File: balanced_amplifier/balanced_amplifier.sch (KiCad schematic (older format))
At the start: 11 parts, among them J1 Conn_01x04_Male, J2 Conn_01x04_Male, J3 Screw_Terminal_01x03, J4 Conn_01x04_Male, J5 Conn_01x04_Male

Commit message: update balanced amplifier TODO and swap power connector for molex SL
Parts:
- removed J3: Screw_Terminal_01x03, TerminalBlock_Phoenix:TerminalBlock_Phoenix_PT-1,5-3-5.0-H_1x03_P5.00mm_Horizontal, symbol Connector:Screw_Terminal_01x03
- added J3: Conn_01x03_Male, symbol Connector:Conn_01x03_Male
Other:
- note added: "Mounting holes for 8-32 standoffs\nUse isolated standoffs"
- note added: "TODO:\nswap +/- for either input or output connectors (make consistent)\ncheck pinning of power connector matches power supply\nUpdate date field\nAdd power LED(s)\nchange connectors to support headphone amplifier board"
- note removed: "Mounting holes for 8-32 standoffs"
- note removed: "TODO:\nadd knobs for pots\nswap +/- for either input or output connectors (make consistent)\nchange power connector to 1x3 Molex SL\nUpdate date field\nAdd power LED(s)\nchange connectors to support headphone amplifier board\nshould mounting holes be tied to GNDA?"
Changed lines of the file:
@@
-$EndComp
-$Comp
-L Connector:Screw_Terminal_01x03 J3
-U 1 1 5C512EBE
-P 1400 5300
-F 0 "J3" H 1400 5500 50  0000 C CNN
-F 1 "Screw_Terminal_01x03" H 1400 5050 50  0000 C CNN
-F 2 "TerminalBlock_Phoenix:TerminalBlock_Phoenix_PT-1,5-3-5.0-H_1x03_P5.00mm_Horizontal" H 1400 5300 50  0001 C CNN
-F 3 "https://media.digikey.com/pdf/Data%20Sheets/Phoenix%20Contact%20PDFs/1935174.pdf" H 1400 5300 50  0001 C CNN
-F 4 "Phoenix" H 1400 5300 50  0001 C CNN "Manufacturer"
-F 5 "1935174" H 1400 5300 50  0001 C CNN "Manufacturer PN"
-F 6 "Digikey" H 1400 5300 50  0001 C CNN "Distributor"
-F 7 "277-1578-ND" H 1400 5300 50  0001 C CNN "Distributor PN"
-F 8 "https://www.digikey.com/product-detail/en/phoenix-contact/1935174/277-1578-ND/568615" H 1400 5300 50  0001 C CNN "URL"
-F 9 "0.60" H 1400 5300 50  0001 C CNN "Unit Price"
-	1    1400 5300
-	-1   0    0    1
 $EndComp
 $Comp
@@
 	9300 3450 9200 3450
 Text Notes 900  1500 0    50   ~ 0
-TODO:\nadd knobs for pots\nswap +/- for either input or output connectors (make consistent)\nchange power connector to 1x3 Molex SL\nUpdate date field\nAdd power LED(s)\nchange connectors to support headphone amplifier board\nshould mounting holes be tied to GNDA?
+TODO:\nswap +/- for either input or output connectors (make consistent)\ncheck pinning of power connector matches power supply\nUpdate date field\nAdd power LED(s)\nchange connectors to support headphone amplifier board
 Text Label 1450 2600 0    50   ~ 0
 right_in_hot
@@
 $EndComp
 Text Notes 7850 5450 0    50   ~ 0
-Mounting holes for 8-32 standoffs
+Mounting holes for 8-32 standoffs\nUse isolated standoffs
+$Comp
+L Connector:Conn_01x03_Male J3
+U 1 1 5CFE6E45
+P 1400 5300
+F 0 "J3" H 1372 5232 50  0000 R CNN
+F 1 "Conn_01x03_Male" H 1372 5323 50  0000 R CNN
+F 2 "" H 1400 5300 50  0001 C CNN
+F 3 "~" H 1400 5300 50  0001 C CNN
+	1    1400 5300
+	1    0    0    1
+$EndComp
 $EndSCHEMATC

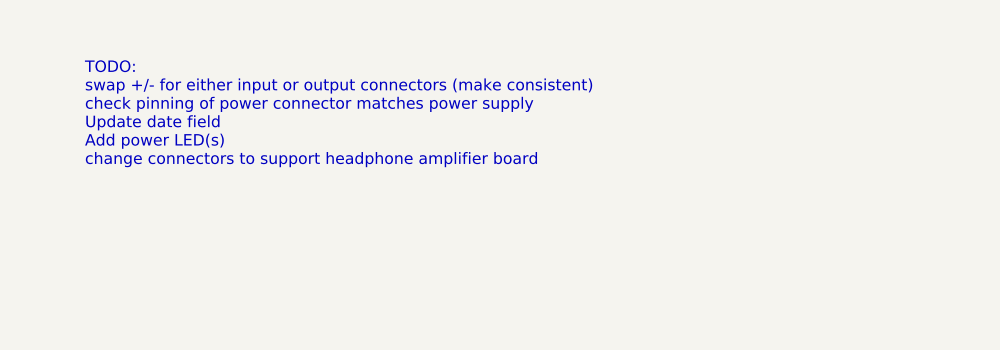
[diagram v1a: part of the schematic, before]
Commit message: update balanced amplifier TODO
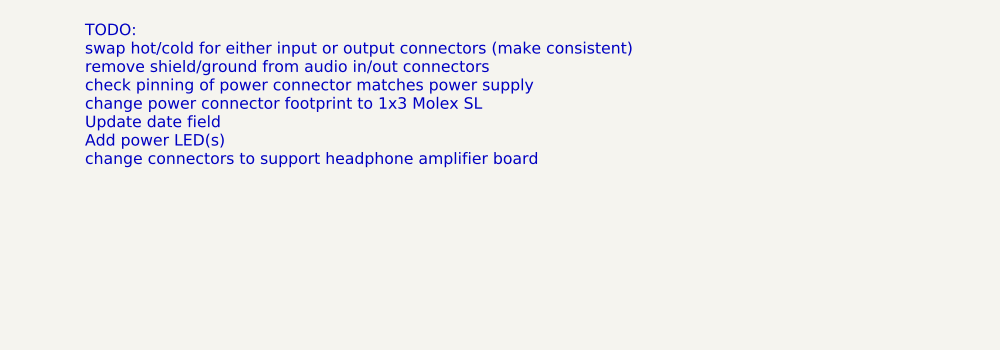
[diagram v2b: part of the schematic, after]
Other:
- note added: "TODO:\nswap hot/cold for either input or output connectors (make consistent)\nremove shield/ground from audio in/out connectors\ncheck pinning of power connector matches power supply\nchange power connector footprint to 1x3 Molex SL\nUpdate date field\nAdd power LED(s)\nchange connectors to support headphone amplifier board"
- note removed: "TODO:\nswap +/- for either input or output connectors (make consistent)\ncheck pinning of power connector matches power supply\nUpdate date field\nAdd power LED(s)\nchange connectors to support headphone amplifier board"
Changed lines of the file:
@@
 	9300 3450 9200 3450
 Text Notes 900  1500 0    50   ~ 0
-TODO:\nswap +/- for either input or output connectors (make consistent)\ncheck pinning of power connector matches power supply\nUpdate date field\nAdd power LED(s)\nchange connectors to support headphone amplifier board
+TODO:\nswap hot/cold for either input or output connectors (make consistent)\nremove shield/ground from audio in/out connectors\ncheck pinning of power connector matches power supply\nchange power connector footprint to 1x3 Molex SL\nUpdate date field\nAdd power LED(s)\nchange connectors to support headphone amplifier board
 Text Label 1450 2600 0    50   ~ 0
 right_in_hot

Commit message: update balanced amplifier input/output/power connectors
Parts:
- removed J2, J4, J5: Conn_01x04_Male, Connector_Molex_SL:Molex_SL_A-70543-0003_1x04_P2.54mm_Vertical, symbol Connector:Conn_01x04_Male
- removed J3: Conn_01x03_Male, symbol Connector:Conn_01x03_Male
- added J2, J4, J5, J6, J7: Molex_SL_01x02_Male, Connector_Molex_SL:Molex_SL_A-70543-0001_1x02_P2.54mm_Vertical, symbol Connector_gkeeth:Molex_SL_01x02_Male
- added J3: Molex_SL_01x03_Male, Connector_Molex_SL:Molex_SL_A-70543-0002_1x03_P2.54mm_Vertical, symbol Connector_gkeeth:Molex_SL_01x03_Male
- J1: value Conn_01x04_Male -> Molex_SL_01x02_Male; footprint Connector_Molex_SL:Molex_SL_A-70543-0003_1x04_P2.54mm_Vertical -> Connector_Molex_SL:Molex_SL_A-70543-0001_1x02_P2.54mm_Vertical; symbol Connector:Conn_01x04_Male -> Connector_gkeeth:Molex_SL_01x02_Male; Distributor PN WM4802-ND -> (none); Manufacturer PN 0705430003 -> 0705430001; URL https://www.digikey.com/products/en?keywords=0705430003 -> (none); Unit Price 0.99 -> (none)
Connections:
- net GNDA: now also J3.2 (Pin_2)
- net VCC: now also J3.1 (Pin_1)
- net VEE: now also J3.3 (Pin_3)
- net left_in_cold: now also J2.2 (Pin_2)
- net left_in_hot: now also J2.1 (Pin_1)
- net right_in_cold: now also J1.2 (Pin_2); no longer J1.4 (Pin_4)
- removed net right_in_ground: J1.2 (Pin_2), J1.3 (Pin_3)
- new net left_out_cold: J6.2 (Pin_2), J7.2 (Pin_2)
- new net left_out_hot: J6.1 (Pin_1), J7.1 (Pin_1)
- new net right_out_cold: J4.2 (Pin_2), J5.2 (Pin_2)
- new net right_out_hot: J4.1 (Pin_1), J5.1 (Pin_1)
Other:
- note added: "MOUNTING HOLES"
- note added: "TODO:\nUpdate date field\nAdd power LED(s)"
- note added: "Use insulating 8-32 standoffs"
- note added: "duplicate output connectors for\ninput/output board and headphone amplifier board"
- note added: "hot/cold outputs swapped to maintain overall phase\n(volume control inverts)"
- note removed: "Mounting holes for 8-32 standoffs\nUse isolated standoffs"
- note removed: "TODO:\nswap hot/cold for either input or output connectors (make consistent)\nremove shield/ground from audio in/out connectors\ncheck pinning of power connector matches power supply\nchange power connector footprint to 1x3 Molex SL\nUpdate date field\nAdd power LED(s)\nchange connectors to support headphone amplifier board"
- note removed: "hot/cold inputs swapped to maintain overall phase\n(volume control inverts)"
- moved on the sheet: C100, C101, H1, H2, H3, H4

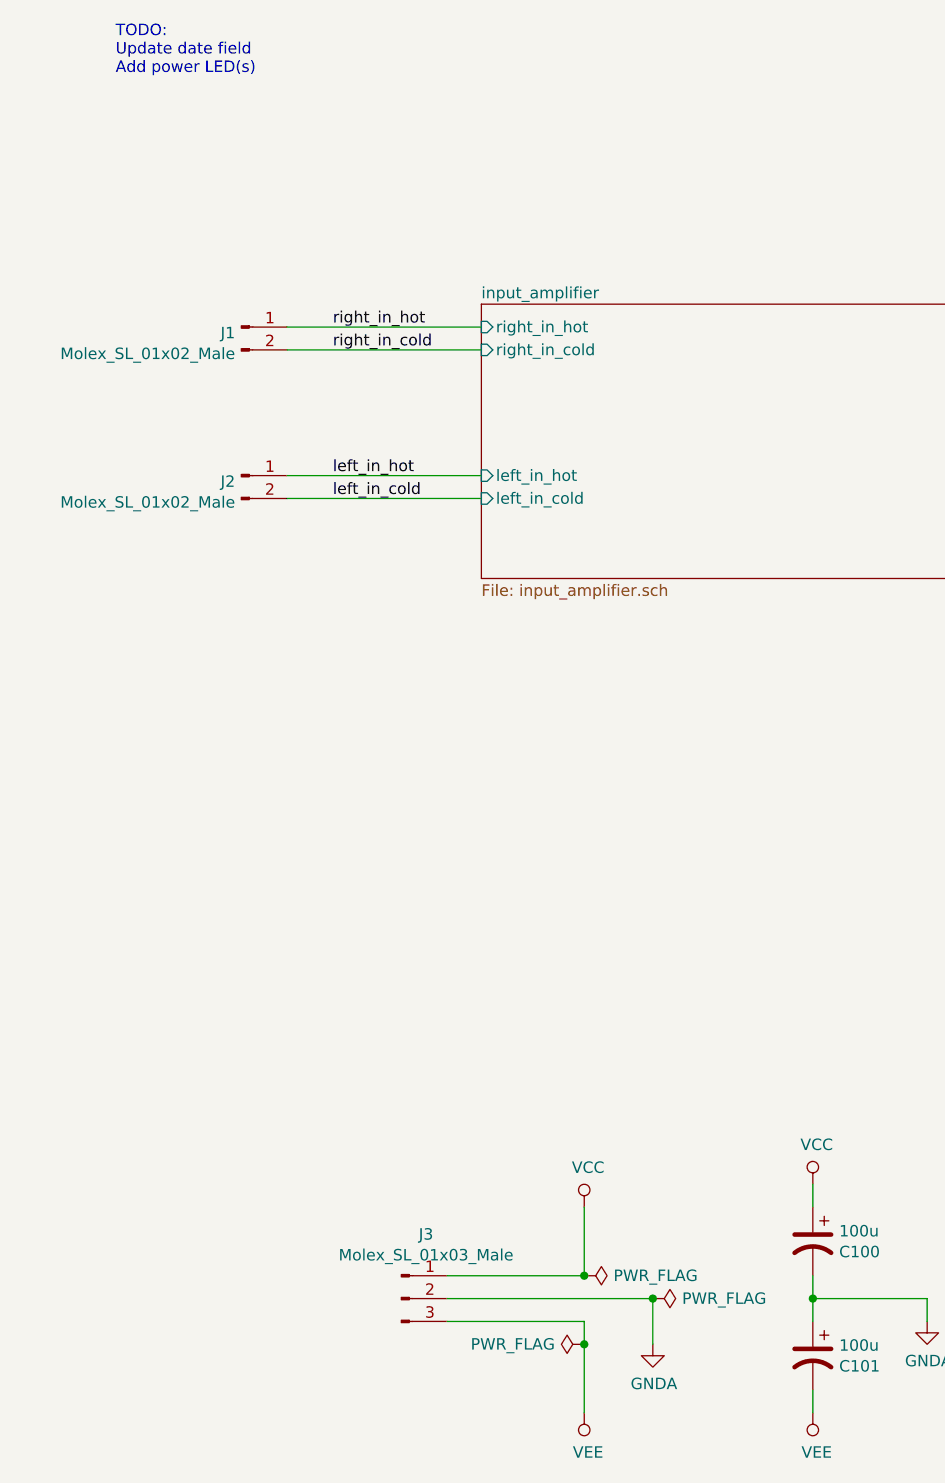
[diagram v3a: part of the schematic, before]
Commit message: update TODO and title block
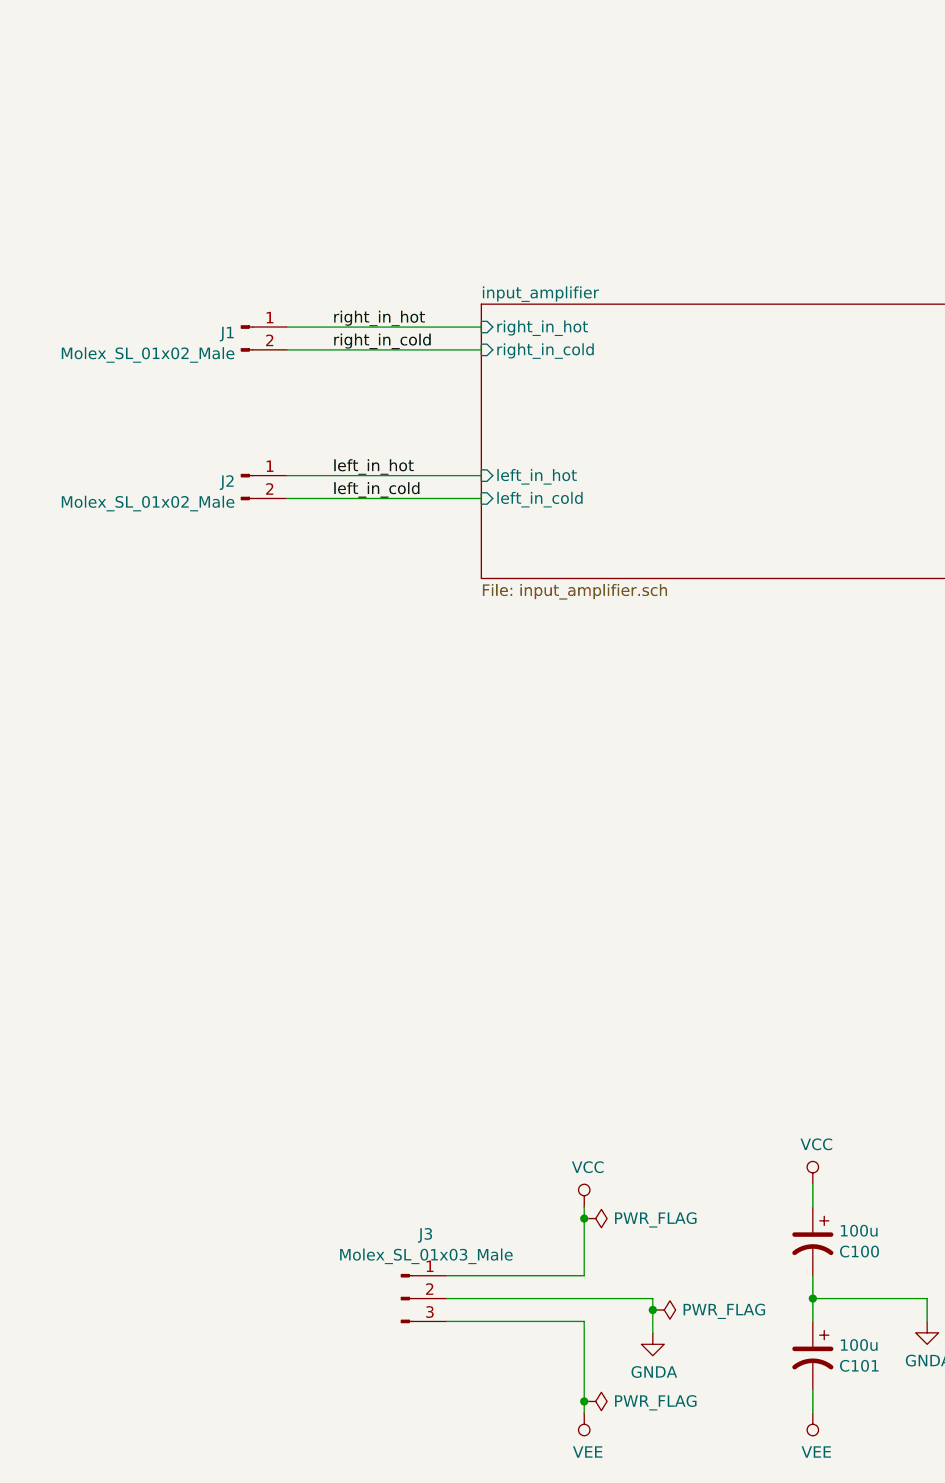
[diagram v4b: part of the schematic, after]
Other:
- note removed: "TODO:\nUpdate date field\nAdd power LED(s)"
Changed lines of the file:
@@
 encoding utf-8
 Sheet 1 3
-Title "Volume Control / Balance Control for Preamp 2019"
-Date "2019-01-14"
+Title "Balanced Amplifier"
+Date "2019-06-18"
 Rev "1"
 Comp "G. Keeth"
-Comment1 ""
+Comment1 "Preamp 2019"
 Comment2 ""
 Comment3 ""
@@
 $EndComp
 Wire Wire Line
-	2950 7350 2950 7050
+	2950 7350 2950 7300
 Wire Wire Line
 	2950 6950 2350 6950
@@
 	2350 6750 2950 6750
 Wire Wire Line
-	2950 6750 2950 6450
+	2950 6750 2950 6500
 $Comp
 L power:GNDA #PWR?
 U 1 1 5C5131A4
-P 3250 7050
+P 3250 7000
 AR Path="/5BE4EEC1/5C5131A4" Ref="#PWR?"  Part="1"
 AR Path="/5C5131A4" Ref="#PWR0136"  Part="1"
-F 0 "#PWR0136" H 3250 6800 50  0001 C CNN
-F 1 "GNDA" H 3255 6877 50  0000 C CNN
-F 2 "" H 3250 7050 50  0001 C CNN
-F 3 "" H 3250 7050 50  0001 C CNN
-	1    3250 7050
-	1    0    0    -1
-$EndComp
-Wire Wire Line
-	3250 7050 3250 6850
+F 0 "#PWR0136" H 3250 6750 50  0001 C CNN
+F 1 "GNDA" H 3255 6827 50  0000 C CNN
+F 2 "" H 3250 7000 50  0001 C CNN
+F 3 "" H 3250 7000 50  0001 C CNN
+	1    3250 7000
+	1    0    0    -1
+$EndComp
+Wire Wire Line
+	3250 7000 3250 6900
 Wire Wire Line
 	3250 6850 2350 6850
-Text Notes 900  1500 0    50   ~ 0
-TODO:\nUpdate date field\nAdd power LED(s)
 Text Label 1850 3250 0    50   ~ 0
 left_in_hot
@@
 L power:PWR_FLAG #FLG0101
 U 1 1 5C227712
-P 2950 6750
-F 0 "#FLG0101" H 2950 6825 50  0001 C CNN
-F 1 "PWR_FLAG" V 2950 6878 50  0000 L CNN
-F 2 "" H 2950 6750 50  0001 C CNN
-F 3 "~" H 2950 6750 50  0001 C CNN
-	1    2950 6750
+P 2950 6500
+F 0 "#FLG0101" H 2950 6575 50  0001 C CNN
+F 1 "PWR_FLAG" V 2950 6628 50  0000 L CNN
+F 2 "" H 2950 6500 50  0001 C CNN
+F 3 "~" H 2950 6500 50  0001 C CNN
+	1    2950 6500
 	0    1    1    0
 $EndComp
-Connection ~ 3250 6850
-Connection ~ 2950 6750
 $Comp
 L power:PWR_FLAG #FLG0102
 U 1 1 5C22777E
-P 3250 6850
-F 0 "#FLG0102" H 3250 6925 50  0001 C CNN
-F 1 "PWR_FLAG" V 3250 6978 50  0000 L CNN
-F 2 "" H 3250 6850 50  0001 C CNN
-F 3 "~" H 3250 6850 50  0001 C CNN
-	1    3250 6850
+P 3250 6900
+F 0 "#FLG0102" H 3250 6975 50  0001 C CNN
+F 1 "PWR_FLAG" V 3250 7028 50  0000 L CNN
+F 2 "" H 3250 6900 50  0001 C CNN
+F 3 "~" H 3250 6900 50  0001 C CNN
+	1    3250 6900
 	0    1    1    0
 $EndComp
@@
 L power:PWR_FLAG #FLG0103
 U 1 1 5C227797
-P 2950 7050
-F 0 "#FLG0103" H 2950 7125 50  0001 C CNN
-F 1 "PWR_FLAG" V 2950 7178 50  0000 L CNN
-F 2 "" H 2950 7050 50  0001 C CNN
-F 3 "~" H 2950 7050 50  0001 C CNN
-	1    2950 7050
-	0    -1   1    0
-$EndComp
-Connection ~ 2950 7050
-Wire Wire Line
-	2950 7050 2950 6950
+P 2950 7300
+F 0 "#FLG0103" H 2950 7375 50  0001 C CNN
+F 1 "PWR_FLAG" V 2950 7428 50  0000 L CNN
+F 2 "" H 2950 7300 50  0001 C CNN
+F 3 "~" H 2950 7300 50  0001 C CNN
+	1    2950 7300
+	0    1    1    0
+$EndComp
 $Comp
 L Mechanical:MountingHole_Pad H2
@@
 Text Notes 8350 5350 0    50   Italic 10
 MOUNTING HOLES
+Connection ~ 2950 6500
+Wire Wire Line
+	2950 6500 2950 6450
+Wire Wire Line
+	2950 6950 2950 7300
+Connection ~ 2950 7300
+Connection ~ 3250 6900
+Wire Wire Line
+	3250 6900 3250 6850
 $EndSCHEMATC

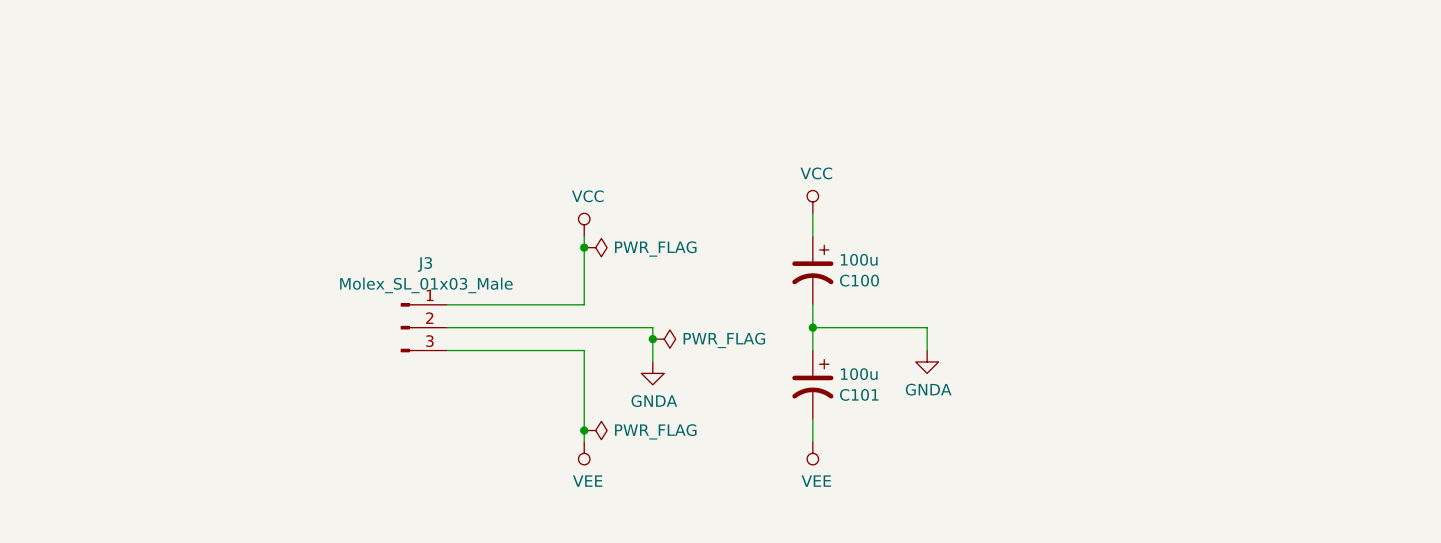
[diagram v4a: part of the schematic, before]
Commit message: add license info to schematics & layouts, including made with kicad logo, as well as project info to silkscreen
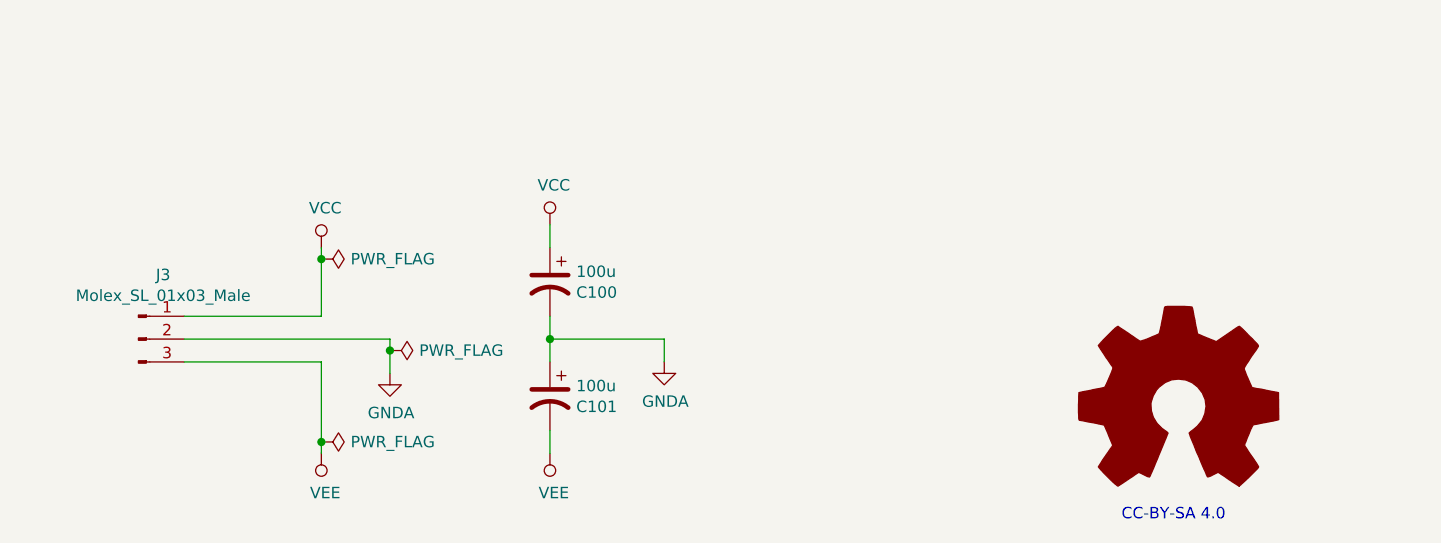
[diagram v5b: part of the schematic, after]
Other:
- note added: "CC-BY-SA 4.0"
- moved on the sheet: C100, C101, J3
